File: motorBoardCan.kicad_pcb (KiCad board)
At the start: 6 copper layers, 50 x 50 mm, 45 parts, among them J1 Conn_01x04_Pin, J2 Conn_01x04_Pin, J3 Conn_02x04_Top_Bottom, J4 Conn_01x02_Socket, J5 Conn_01x02_Socket, J6 Conn_02x04_Top_Bottom, U1 NUCLEO-G431KB, U10 TPS563200, U2 LMD18200, U4 SN65HVD230, U5 LD1117S33TR_SOT223, U6 LMD18200

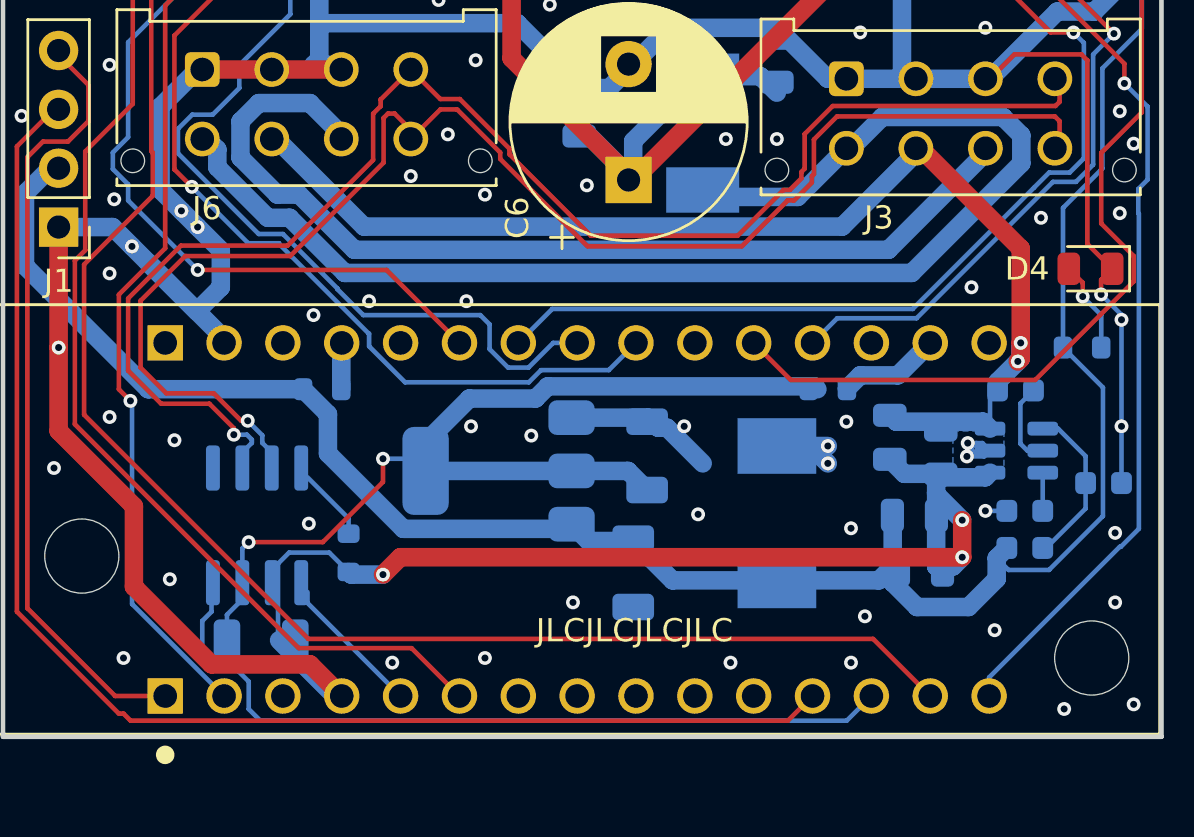
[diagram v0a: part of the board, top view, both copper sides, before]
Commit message: Add option 12V Elec + add missing brake pullups
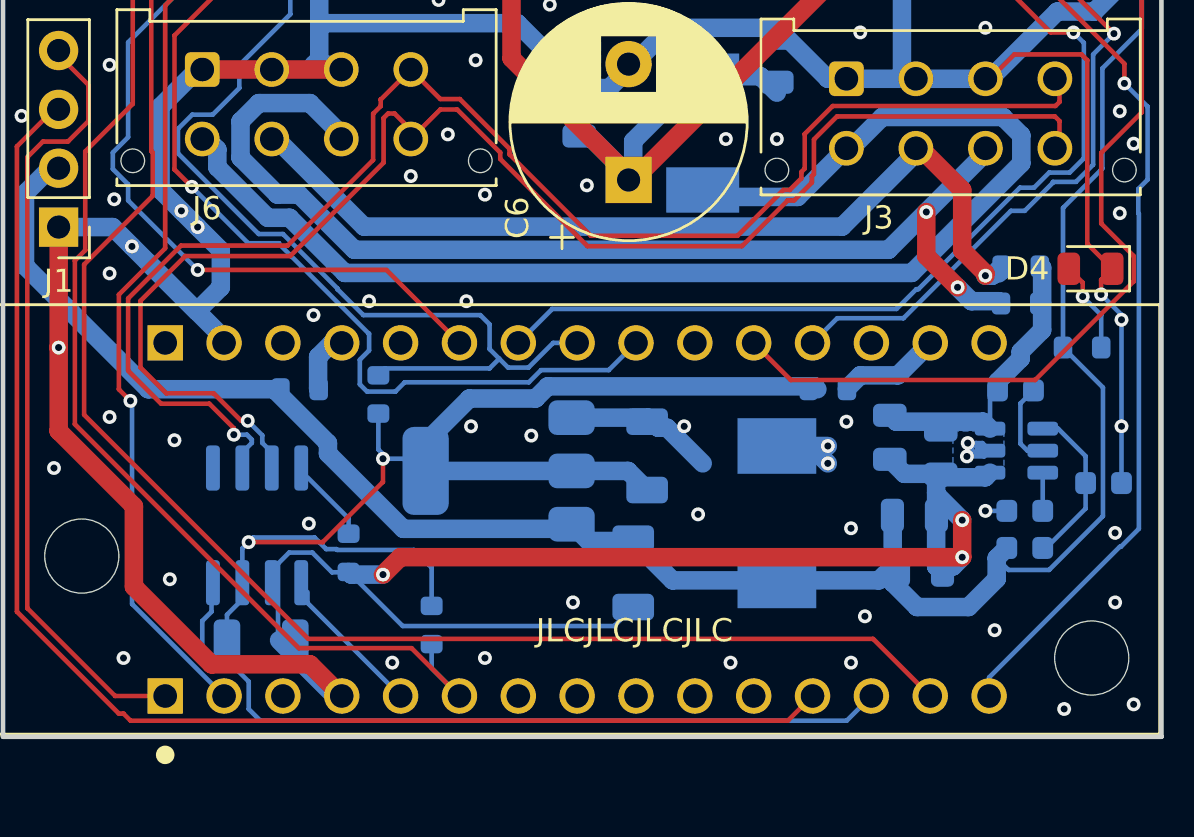
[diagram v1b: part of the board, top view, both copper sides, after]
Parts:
- added R10: 10kR, Resistor_SMD:R_0603_1608Metric, B.Cu at (93.0, 92.6)
- added R7: 0R, Resistor_SMD:R_0603_1608Metric, B.Cu at (120.7, 88.7)
- added R8: DNP, Resistor_SMD:R_0603_1608Metric, B.Cu at (120.7, 87.1)
- added R9: 10kR, Resistor_SMD:R_0603_1608Metric, B.Cu at (95.3, 102.6)
- moved R6 0.98 mm to (89.6, 92.4)
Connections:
- C21 pad 1: 12V_POW_P -> /DCDC_5V/Vin_for_DCDC_logic
- C22 pad 1: 12V_POW_P -> /DCDC_5V/Vin_for_DCDC_logic
- R36 pad 1: 12V_POW_P -> /DCDC_5V/Vin_for_DCDC_logic
- U10 pad 3: 12V_POW_P -> /DCDC_5V/Vin_for_DCDC_logic
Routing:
- net GND: track 198.2 -> 211.8 mm, vias 88 -> 86
- net /DCDC_5V/Vin_for_DCDC_logic: track 0.00 -> 12.5 mm
- net 3.3V: track 43.7 -> 55.9 mm
- net 12V_POW_P: track 50.9 -> 38.9 mm, vias 2 -> 1
- net 12V_ELEC_P: track 42.6 -> 48.6 mm, vias 0 -> 2
- net /BRAKE_A: track 58.3 -> 63.8 mm
- net /BRAKE_B: track 48.4 -> 51.2 mm
- net /PWM_B: track 34.6 -> 36.4 mm
- net 5V: track 95.3 -> 94.6 mm
- net Net-(U1B-+5V): track 2.01 -> 2.68 mm

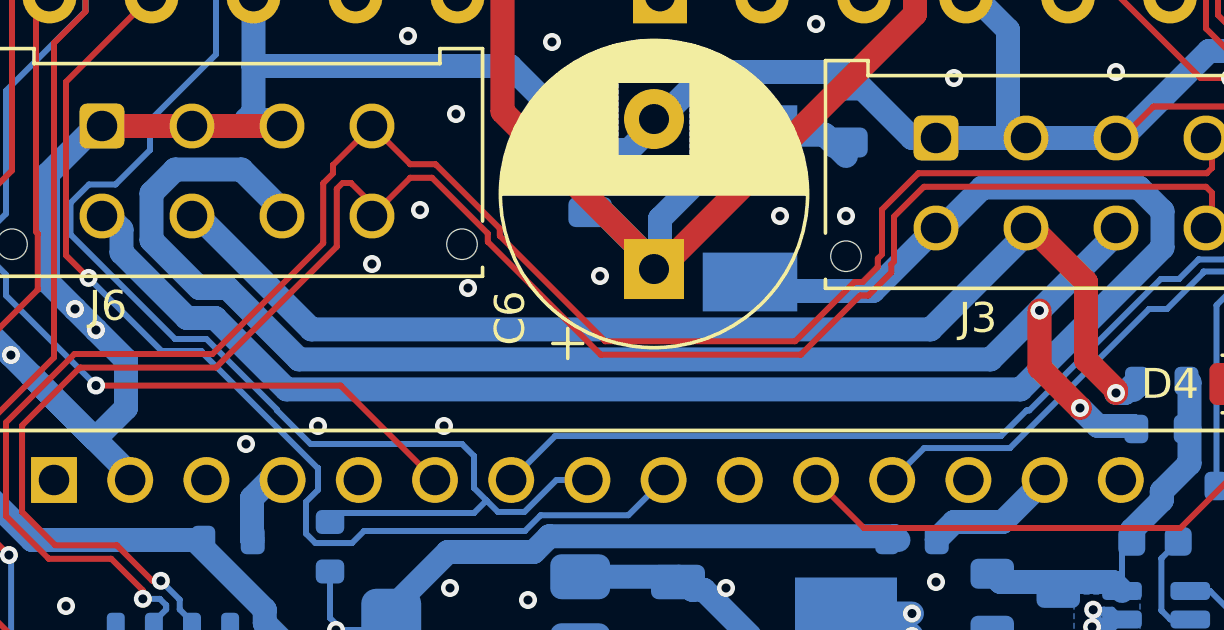
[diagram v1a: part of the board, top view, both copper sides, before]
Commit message: add choice between 12V power and 24V power
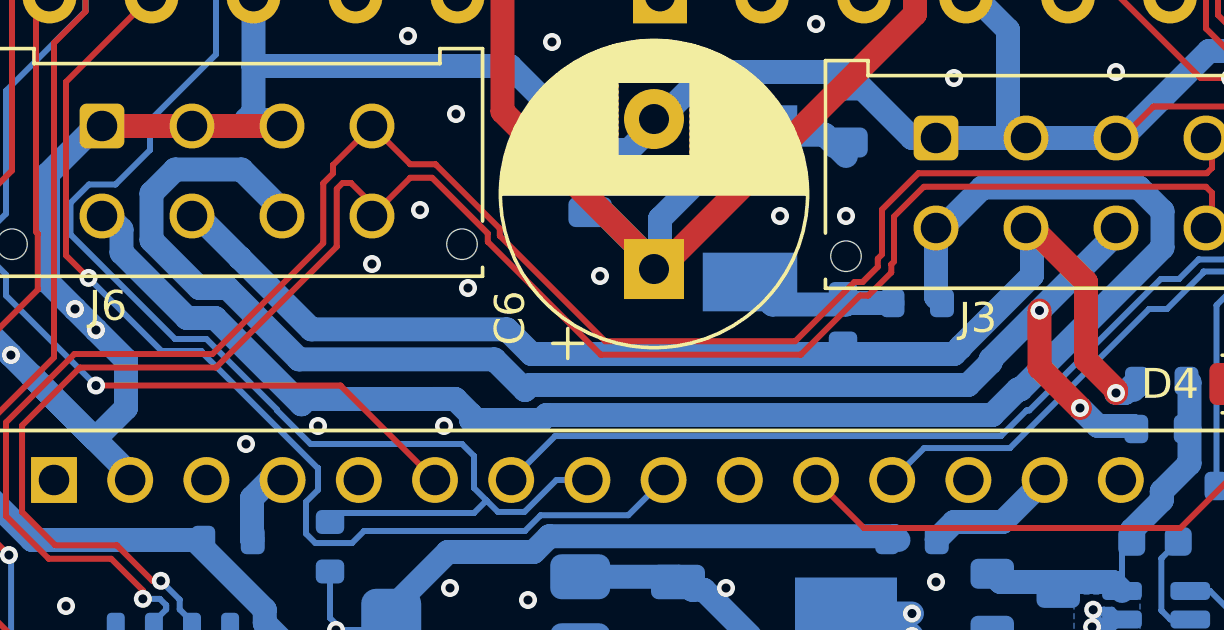
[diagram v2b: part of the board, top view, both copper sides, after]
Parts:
- added R11: DNP, Resistor_SMD:R_0603_1608Metric, B.Cu at (112.6, 84.5)
- added R12: 0R, Resistor_SMD:R_0603_1608Metric, B.Cu at (110.1, 85.0)
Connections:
- F1 pad 2: 24V_POW_P -> Net-(F1-Pad2)
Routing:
- net Net-(F1-Pad2): track 0.00 -> 5.51 mm
- net 24V_POW_P: track 57.3 -> 53.6 mm
- net 12V_POW_P: track 38.9 -> 40.5 mm
- net 12V_ELEC_P: track 48.6 -> 49.5 mm

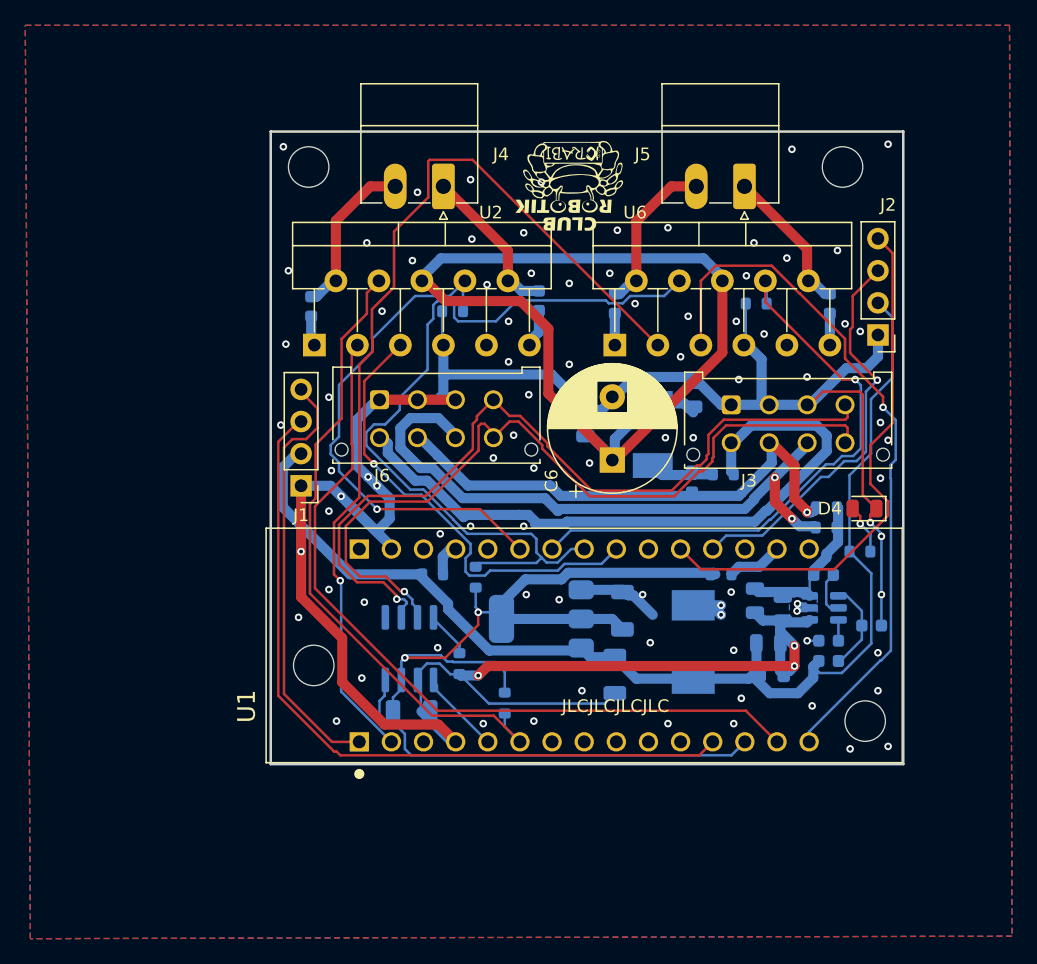
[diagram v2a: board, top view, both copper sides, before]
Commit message: basic routing of C610 connectors
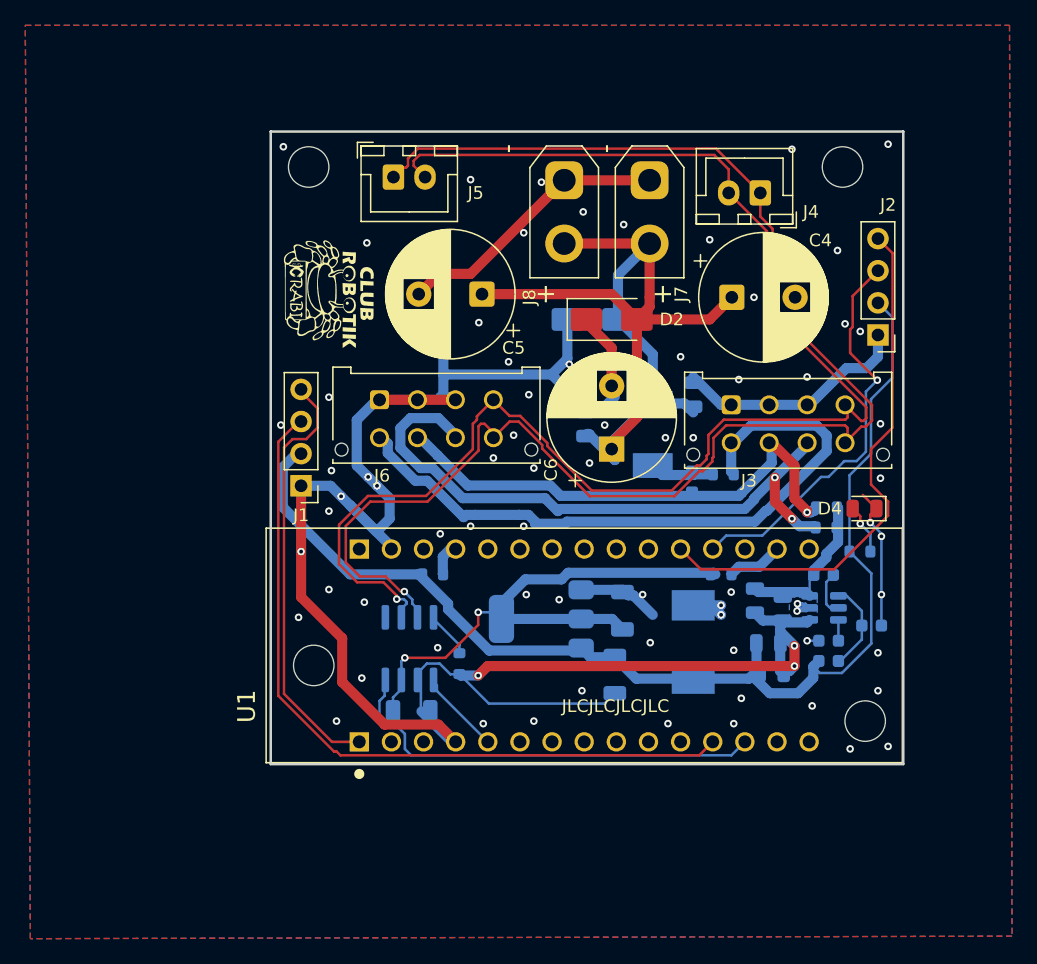
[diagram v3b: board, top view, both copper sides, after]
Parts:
- removed C8, C9: 10nF, Capacitor_SMD:C_0603_1608Metric
- removed R10, R9: 10kR, Resistor_SMD:R_0603_1608Metric
- removed R3, R5: 1kR, Resistor_SMD:R_0603_1608Metric
- removed U2, U6: LMD18200, Package_TO_SOT_THT:TO-220-11_P3.4x5.08mm_StaggerOdd_Lead4.85mm_Vertical
- added D2: D_TVS, Diode_SMD:D_SMA, F.Cu at (103.8, 72.2)
- added D3: D_TVS, Diode_SMD:D_SMA, B.Cu at (102.2, 72.2)
- added J7: Conn_01x02_Pin, Connector_AMASS:AMASS_XT30UPB-F_1x02_P5.0mm_Vertical, F.Cu at (106.8, 61.2)
- added J8: Conn_01x02_Pin, Connector_AMASS:AMASS_XT30UPB-F_1x02_P5.0mm_Vertical, F.Cu at (100.0, 61.2)
- C4, C5: value 10nF -> C_Polarized; footprint Capacitor_SMD:C_0603_1608Metric -> Capacitor_THT:CP_Radial_D10.0mm_P5.00mm; moved to F.Cu
- J4, J5: value Conn_01x02_Socket -> Conn_01x02_Pin; footprint Connector_Phoenix_MC:PhoenixContact_MC_1,5_2-G-3.81_1x02_P3.81mm_Horizontal -> Connector_JST:JST_XH_B2B-XH-A_1x02_P2.50mm_Vertical
- moved C4 33.3 mm to (113.2, 70.5), turned to 0 degrees
- moved J5 27.8 mm to (86.5, 61.0), turned to 0 degrees
- moved J4 25.1 mm to (115.5, 62.2)
- moved G*** 20.7 mm to (81.5, 70.2), turned to -90 degrees
- moved G*** 19.5 mm to (82.2, 69.5)
- moved C5 4.53 mm to (93.5, 70.2), turned to 180 degrees
- moved C6 0.87 mm to (103.8, 82.5)
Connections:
- C4 pad 1: Net-(J4-Pin_2) -> 24V
- C4 pad 2: Net-(U2-BOOTSTRAP1) -> GND
- C5 pad 1: Net-(U2-BOOTSTRAP2) -> 24V
- C5 pad 2: Net-(J4-Pin_1) -> GND
- J4 pad 1: Net-(J4-Pin_1) -> CAN+
- J4 pad 2: Net-(J4-Pin_2) -> CAN-
- J5 pad 1: Net-(J5-Pin_1) -> CAN+
- J5 pad 2: Net-(J5-Pin_2) -> CAN-
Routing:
- net /DIR_A: track 75.2 -> 0.00 mm, vias 1 -> 0
- net /BRAKE_A: track 63.8 -> 0.00 mm
- net /DIR_B: track 62.2 -> 0.00 mm
- net CAN+: track 63.5 -> 119.7 mm
- net /PWM_A: track 55.8 -> 0.00 mm, vias 1 -> 0
- net CAN-: track 64.4 -> 118.1 mm
- net /BRAKE_B: track 51.2 -> 0.00 mm
- net /CURRENT_A: track 46.8 -> 0.00 mm, vias 1 -> 0
- net /CURRENT_B: track 40.9 -> 0.00 mm, vias 1 -> 0
- net /PWM_B: track 36.4 -> 0.00 mm, vias 1 -> 0
- net Net-(J4-Pin_2): track 12.9 -> 0.00 mm
- net Net-(J5-Pin_2): track 12.5 -> 0.00 mm
- net Net-(J4-Pin_1): track 12.2 -> 0.00 mm
- net 3.3V: track 55.9 -> 43.9 mm
- net Net-(J5-Pin_1): track 11.5 -> 0.00 mm
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
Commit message: small tuning
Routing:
- net GND: track 215.2 -> 208.2 mm, vias 71 -> 70
- net 24V: track 72.7 -> 71.9 mm
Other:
- board text added: "Coupe 2025/2026 Carte moteur C610"
- board text removed: "Coupe 2024/2025 Carte moteur"
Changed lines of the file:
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@@
 		)
 	)
-	(gr_text "Coupe 2024/2025 Carte moteur"
+	(gr_text "Coupe 2025/2026 Carte moteur C610"
 		(locked yes)
 		(at 114.8 87.4 0)
@@
 	)
 	(via
-		(at 123.4 73.2)
-		(size 0.6)
-		(drill 0.3)
-		(layers "F.Cu" "B.Cu")
-		(free yes)
-		(net 1)
-	)
-	(via
 		(at 97.6 84)
 		(size 0.6)
@@
 	)
 	(segment
-		(start 90.45 76.6)
-		(end 99 76.6)
-		(width 0.8)
-		(layer "B.Cu")
-		(net 1)
-	)
-	(segment
 		(start 82.365 86.235)
 		(end 81.53 85.4)
@@
 	)
 	(segment
-		(start 118.6 79)
-		(end 112.4 79)
-		(width 0.8)
-		(layer "B.Cu")
-		(net 1)
-	)
-	(segment
-		(start 90.45 78.15)
-		(end 90.45 76.6)
+		(start 92.9 76.6)
+		(end 99 76.6)
 		(width 0.8)
 		(layer "B.Cu")
@@
 	)
 	(segment
-		(start 103.8 78.567677)
-		(end 102.867677 79.5)
+		(start 100.25 72.25)
+		(end 100.25 75.35)
 		(width 0.8)
 		(layer "B.Cu")
@@
 	)
 	(segment
-		(start 100.25 72.25)
-		(end 100.25 75.35)
+		(start 91.83 100.4)
+		(end 91.715 100.285)
 		(width 0.8)
 		(layer "B.Cu")
@@
 	)
 	(segment
-		(start 91.83 100.4)
-		(end 91.715 100.285)
+		(start 91.4 78.1)
+		(end 92.9 76.6)
 		(width 0.8)
 		(layer "B.Cu")
@@
 	)
 	(segment
-		(start 112.4 79)
-		(end 110.2 76.8)
-		(width 0.8)
-		(layer "B.Cu")
-		(net 1)
-	)
-	(segment
 		(start 94.049 102.619)
 		(end 103.181 102.619)
@@
 	)
 	(segment
+		(start 110.4 77.05)
+		(end 110.2 77.25)
+		(width 0.2)
+		(layer "B.Cu")
+		(net 1)
+	)
+	(segment
 		(start 91.7 100.3)
 		(end 91 100.3)
@@
 	)
 	(segment
-		(start 101.8 79.4)
-		(end 102.967677 79.4)
-		(width 0.8)
-		(layer "B.Cu")
-		(net 1)
-	)
-	(segment
 		(start 91 100.3)
 		(end 90.151143 99.451143)
@@
 	)
 	(segment
-		(start 117.075 96.85)
-		(end 117.075 96.925)
+		(start 101.85 79.4)
+		(end 103.75 77.5)
 		(width 0.8)
 		(layer "B.Cu")
@@
 	)
 	(segment
-		(start 90.2 78.4)
-		(end 90.45 78.15)
+		(start 117.075 96.85)
+		(end 117.075 96.925)
 		(width 0.8)
 		(layer "B.Cu")
@@
 	)
 	(segment
-		(start 90.2 78.4)
-		(end 91.4 78.4)
-		(width 0.8)
-		(layer "B.Cu")
-		(net 1)
-	)
-	(segment
 		(start 125.075 94)
 		(end 125.075 89.4)
@@
 	)
 	(segment
-		(start 90.45 76.6)
-		(end 90.45 74)
-		(width 0.8)
-		(layer "B.Cu")
-		(net 1)
-	)
-	(segment
 		(start 85.4 78.4)
 		(end 83.6 80.2)
@@
 	)
 	(segment
-		(start 110.4 76.8)
-		(end 110.2 76.8)
+		(start 88.67 103.19)
+		(end 88.715 103.235)
 		(width 0.2)
 		(layer "B.Cu")
@@
 	)
 	(segment
-		(start 88.67 103.19)
-		(end 88.715 103.235)
-		(width 0.2)
+		(start 101.8 79.4)
+		(end 101.85 79.4)
+		(width 0.8)
 		(layer "B.Cu")
 		(net 1)
 	)
 	(segment
-		(start 85.2 85.4)
-		(end 86.2 86.4)
+		(start 112.4 79)
+		(end 118.6 79)
 		(width 0.8)
 		(layer "B.Cu")
@@
 	)
 	(segment
-		(start 102.967677 79.4)
-		(end 104 78.367677)
+		(start 110.65 77.25)
+		(end 112.4 79)
+		(width 0.8)
+		(layer "B.Cu")
+		(net 1)
+	)
+	(segment
+		(start 85.2 85.4)
+		(end 86.2 86.4)
 		(width 0.8)
 		(layer "B.Cu")
@@
 	)
 	(segment
+		(start 91.4 78.4)
+		(end 91.4 78.1)
+		(width 0.8)
+		(layer "B.Cu")
+		(net 1)
+	)
+	(segment
+		(start 110.2 77.25)
+		(end 110.65 77.25)
+		(width 0.8)
+		(layer "B.Cu")
+		(net 1)
+	)
+	(segment
 		(start 115.075 95.425)
 		(end 115.7 96.05)
@@
 	)
 	(segment
-		(start 100 66.25)
-		(end 106.75 66.25)
-		(width 0.8)
-		(layer "F.Cu")
-		(net 31)
-	)
-	(segment
 		(start 103.75 70.25)
 		(end 93.5 70.25)
@@
 	)
 	(segment
-		(start 104 83.367677)
+		(start 104 81.69)
+		(end 106.8 78.89)
+		(width 0.8)
+		(layer "B.Cu")
+		(net 31)
+	)
+	(segment
+		(start 104 82.75)
 		(end 104 81.69)
 		(width 0.8)
@@
 	)
 	(segment
-		(start 106.8 78.89)
-		(end 109.49 78.89)
+		(start 107 78.89)
+		(end 107 75)
 		(width 0.8)
 		(layer "B.Cu")
@@
 	)
 	(segment
-		(start 101.8 81.3)
-		(end 101.932323 81.3)
+		(start 109.49 78.89)
+		(end 110.2 79.6)
 		(width 0.8)
 		(layer "B.Cu")
@@
 	)
 	(segment
-		(start 107 78.89)
-		(end 107 75)
+		(start 100 66.25)
+		(end 106.75 66.25)
 		(width 0.8)
 		(layer "B.Cu")
@@
 	)
 	(segment
-		(start 109.49 78.89)
-		(end 110.2 79.6)
+		(start 101.67 81.47)
+		(end 102.72 81.47)
 		(width 0.8)
 		(layer "B.Cu")
@@
 	)
 	(segment
-		(start 101.932323 81.3)
-		(end 104 83.367677)
+		(start 102.72 81.47)
+		(end 104 82.75)
 		(width 0.8)
 		(layer "B.Cu")
@@
 	)
 	(segment
-		(start 104 81.69)
-		(end 106.8 78.89)
+		(start 106.8 78.89)
+		(end 109.49 78.89)
 		(width 0.8)
 		(layer "B.Cu")

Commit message: serigraphy
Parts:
- moved J5 7.07 mm to (93.5, 62.0), turned to 180 degrees
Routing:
- net CAN+: track 119.7 -> 112.8 mm
- net CAN-: track 118.1 -> 115.9 mm
- net GND: vias 70 -> 69
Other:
- board text added: "H"
- board text added: "L"
